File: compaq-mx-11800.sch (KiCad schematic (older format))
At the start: 246 parts, among them J1 Conn_01x16_Female, J2 Conn_01x16_Female, j1 MX-NoLED, k1 MX-NoLED, m1 MX-NoLED, p1 MX-NoLED, q1 MX-NoLED, t1 MX-NoLED, u1 MX-NoLED, x1 MX-NoLED, y1 MX-NoLED

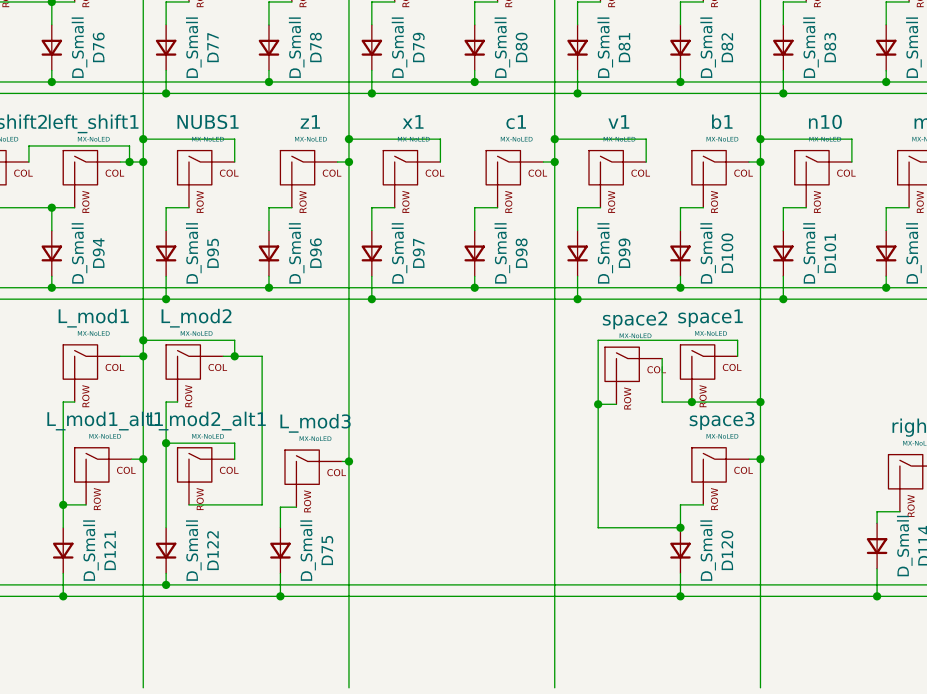
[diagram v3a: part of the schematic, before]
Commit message: revert to using MX_only
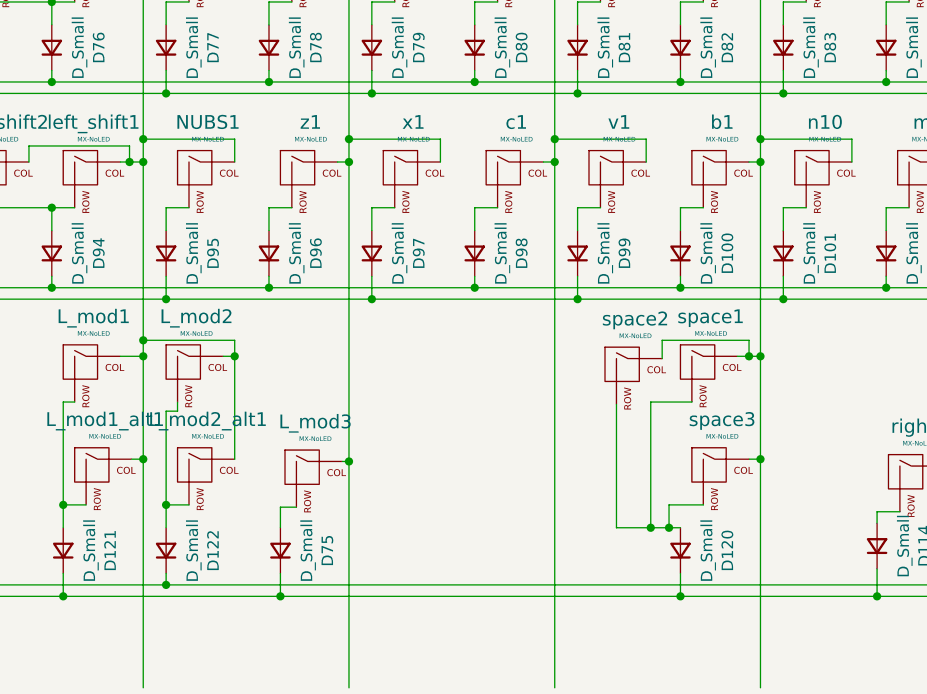
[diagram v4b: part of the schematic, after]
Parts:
- L_mod1, L_mod2, R_mod2, R_mod3: footprint MX_Alps_Hybrid:MX-1.5U-NoLED -> MX_Only:MXOnly-1.5U-NoLED
- L_mod1_alt1, L_mod2_alt1, L_mod3, R_mod1, R_mod2_alt1, R_mod3_alt1: footprint MX_Alps_Hybrid:MX-1.25U-NoLED -> MX_Only:MXOnly-1.25U-NoLED
- space1: footprint MX_Alps_Hybrid:MX-7U-NoLED -> MX_Only:MXOnly-7U-NoLED
- space2, space3: footprint MX_Alps_Hybrid:MX-6.25U-NoLED -> MX_Only:MXOnly-6.25U-NoLED
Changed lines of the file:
@@
 F 0 "L_mod2" H 9483 13823 60  0000 C CNN
 F 1 "MX-NoLED" H 9483 13749 20  0000 C CNN
-F 2 "MX_Alps_Hybrid:MX-1.5U-NoLED" H 8825 13575 60  0001 C CNN
+F 2 "MX_Only:MXOnly-1.5U-NoLED" H 8825 13575 60  0001 C CNN
 F 3 "" H 8825 13575 60  0001 C CNN
 	1    9450 13600
@@
 F 0 "space1" H 11733 13823 60  0000 C CNN
 F 1 "MX-NoLED" H 11733 13749 20  0000 C CNN
-F 2 "MX_Alps_Hybrid:MX-7U-NoLED" H 11075 13575 60  0001 C CNN
+F 2 "MX_Only:MXOnly-7U-NoLED" H 11075 13575 60  0001 C CNN
 F 3 "" H 11075 13575 60  0001 C CNN
 	1    11700 13600
@@
 F 0 "space3" H 11783 14273 60  0000 C CNN
 F 1 "MX-NoLED" H 11783 14199 20  0000 C CNN
-F 2 "MX_Alps_Hybrid:MX-6.25U-NoLED" H 11125 14025 60  0001 C CNN
+F 2 "MX_Only:MXOnly-6.25U-NoLED" H 11125 14025 60  0001 C CNN
 F 3 "" H 11125 14025 60  0001 C CNN
 	1    11750 14050
@@
 F 0 "R_mod1" H 13583 14223 60  0000 C CNN
 F 1 "MX-NoLED" H 13583 14149 20  0000 C CNN
-F 2 "MX_Alps_Hybrid:MX-1.25U-NoLED" H 12925 13975 60  0001 C CNN
+F 2 "MX_Only:MXOnly-1.25U-NoLED" H 12925 13975 60  0001 C CNN
 F 3 "" H 12925 13975 60  0001 C CNN
 	1    13550 14000
@@
 F 0 "R_mod2_alt1" H 14033 14223 60  0000 C CNN
 F 1 "MX-NoLED" H 14033 14149 20  0000 C CNN
-F 2 "MX_Alps_Hybrid:MX-1.25U-NoLED" H 13375 13975 60  0001 C CNN
+F 2 "MX_Only:MXOnly-1.25U-NoLED" H 13375 13975 60  0001 C CNN
 F 3 "" H 13375 13975 60  0001 C CNN
 	1    14000 14000
@@
 	14350 10350 14250 10350
 Wire Wire Line
-	9400 13750 9350 13750
-Wire Wire Line
 	13750 12700 13750 13430
 Wire Wire Line
@@
 F 0 "R_mod3_alt1" H 14943 14373 60  0000 C CNN
 F 1 "MX-NoLED" H 14943 14299 20  0000 C CNN
-F 2 "MX_Alps_Hybrid:MX-1.25U-NoLED" H 14285 14125 60  0001 C CNN
+F 2 "MX_Only:MXOnly-1.25U-NoLED" H 14285 14125 60  0001 C CNN
 F 3 "" H 14285 14125 60  0001 C CNN
 	1    14910 14150
@@
 F 0 "R_mod2" H 14013 13823 60  0000 C CNN
 F 1 "MX-NoLED" H 14013 13749 20  0000 C CNN
-F 2 "MX_Alps_Hybrid:MX-1.5U-NoLED" H 13355 13575 60  0001 C CNN
+F 2 "MX_Only:MXOnly-1.5U-NoLED" H 13355 13575 60  0001 C CNN
 F 3 "" H 13355 13575 60  0001 C CNN
 	1    13980 13600
@@
 F 0 "R_mod3" H 14933 13973 60  0000 C CNN
 F 1 "MX-NoLED" H 14933 13899 20  0000 C CNN
-F 2 "MX_Alps_Hybrid:MX-1.5U-NoLED" H 14275 13725 60  0001 C CNN
+F 2 "MX_Only:MXOnly-1.5U-NoLED" H 14275 13725 60  0001 C CNN
 F 3 "" H 14275 13725 60  0001 C CNN
 	1    14900 13750
@@
 F 0 "L_mod1" H 9033 13823 60  0000 C CNN
 F 1 "MX-NoLED" H 9033 13749 20  0000 C CNN
-F 2 "MX_Alps_Hybrid:MX-1.5U-NoLED" H 8375 13575 60  0001 C CNN
+F 2 "MX_Only:MXOnly-1.5U-NoLED" H 8375 13575 60  0001 C CNN
 F 3 "" H 8375 13575 60  0001 C CNN
 	1    9000 13600
@@
 F 0 "L_mod1_alt1" H 9083 14273 60  0000 C CNN
 F 1 "MX-NoLED" H 9083 14199 20  0000 C CNN
-F 2 "MX_Alps_Hybrid:MX-1.25U-NoLED" H 8425 14025 60  0001 C CNN
+F 2 "MX_Only:MXOnly-1.25U-NoLED" H 8425 14025 60  0001 C CNN
 F 3 "" H 8425 14025 60  0001 C CNN
 	1    9050 14050
@@
 F 0 "L_mod2_alt1" H 9533 14273 60  0000 C CNN
 F 1 "MX-NoLED" H 9533 14199 20  0000 C CNN
-F 2 "MX_Alps_Hybrid:MX-1.25U-NoLED" H 8875 14025 60  0001 C CNN
+F 2 "MX_Only:MXOnly-1.25U-NoLED" H 8875 14025 60  0001 C CNN
 F 3 "" H 8875 14025 60  0001 C CNN
 	1    9500 14050
@@
 Wire Wire Line
 	9250 13480 9250 13550
-Wire Wire Line
-	9350 13750 9350 13930
-Wire Wire Line
-	9450 14200 9770 14200
-Wire Wire Line
-	9770 14200 9770 13550
-Wire Wire Line
-	9770 13550 9650 13550
-Connection ~ 9650 13550
-Wire Wire Line
-	9650 14000 9650 13930
-Wire Wire Line
-	9650 13930 9350 13930
-Connection ~ 9350 13930
-Wire Wire Line
-	9350 13930 9350 14300
 $Comp
 L Device:D_Small D75
@@
 F 0 "L_mod3" H 10003 14283 60  0000 C CNN
 F 1 "MX-NoLED" H 10003 14209 20  0000 C CNN
-F 2 "MX_Alps_Hybrid:MX-1.25U-NoLED" H 9345 14035 60  0001 C CNN
+F 2 "MX_Only:MXOnly-1.25U-NoLED" H 9345 14035 60  0001 C CNN
 F 3 "" H 9345 14035 60  0001 C CNN
 	1    9970 14060
@@
 F 0 "space2" H 11403 13833 60  0000 C CNN
 F 1 "MX-NoLED" H 11403 13759 20  0000 C CNN
-F 2 "MX_Alps_Hybrid:MX-6.25U-NoLED" H 10745 13585 60  0001 C CNN
+F 2 "MX_Only:MXOnly-6.25U-NoLED" H 10745 13585 60  0001 C CNN
 F 3 "" H 10745 13585 60  0001 C CNN
 	1    11370 13610
 	1    0    0    -1
 $EndComp
-Connection ~ 11950 13750
-Wire Wire Line
-	11950 13750 11950 14000
-Wire Wire Line
-	11520 13560 11520 13750
-Wire Wire Line
-	11520 13750 11650 13750
-Connection ~ 11650 13750
-Wire Wire Line
-	11650 13750 11950 13750
 Wire Wire Line
 	11900 14000 11950 14000
@@
 	11950 14000 11950 15000
 Wire Wire Line
-	11600 14300 11240 14300
-Wire Wire Line
-	11240 14300 11240 13760
-Wire Wire Line
-	11240 13480 11850 13480
-Wire Wire Line
-	11850 13550 11850 13480
-Wire Wire Line
-	11320 13760 11240 13760
-Connection ~ 11240 13760
-Wire Wire Line
-	11240 13760 11240 13480
-Wire Wire Line
-	11700 14200 11600 14200
-Wire Wire Line
-	11600 14200 11600 14300
-Connection ~ 11600 14300
+	11600 14300 11550 14300
 Wire Wire Line
-	11950 12700 11950 13750
+	11950 12700 11950 13550
 Wire Wire Line
 	8200 14550 9350 14550
@@
 Wire Wire Line
 	8900 8650 10250 8650
+Wire Wire Line
+	9400 13750 9400 13790
+Wire Wire Line
+	9400 13790 9350 13790
+Wire Wire Line
+	9450 14200 9350 14200
+Wire Wire Line
+	9350 13790 9350 14200
+Connection ~ 9350 14200
+Wire Wire Line
+	9350 14200 9350 14300
+Wire Wire Line
+	9650 14000 9650 13550
+Connection ~ 9650 13550
+Wire Wire Line
+	11850 13550 11900 13550
+Connection ~ 11950 13550
+Wire Wire Line
+	11950 13550 11950 14000
+Wire Wire Line
+	11520 13560 11520 13480
+Wire Wire Line
+	11320 13760 11320 14300
+Wire Wire Line
+	11650 13750 11470 13750
+Wire Wire Line
+	11470 13750 11470 14300
+Connection ~ 11470 14300
+Wire Wire Line
+	11470 14300 11320 14300
+Wire Wire Line
+	11700 14200 11550 14200
+Wire Wire Line
+	11550 14200 11550 14300
+Connection ~ 11550 14300
+Wire Wire Line
+	11550 14300 11470 14300
+Wire Wire Line
+	11900 13480 11900 13550
+Wire Wire Line
+	11520 13480 11900 13480
+Connection ~ 11900 13550
+Wire Wire Line
+	11900 13550 11950 13550
 $EndSCHEMATC

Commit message: update diode footprint
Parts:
- D10, D100, D101, D102, D103, D104, D105, D107, D108, D11, D114, D115, D116, D117, D118, D12, D120, D121, D122, D124, D13, D14, D15, D16, D18, D19, D2, D20, D21, D22, D23, D24, D25, D26, D27, D28, D29, D3, D30, D31, D32, D33, D34, D35, D36, D37, D38, D39, D4, D40, D41, D42, D43, D44, D45, D46, D47, D48, D49, D5, D51, D53, D54, D55, D56, D57, D58, D59, D6, D60, D61, D62, D63, D64, D65, D66, D67, D68, D69, D7, D70, D71, D72, D73, D74, D75, D76, D77, D78, D79, D8, D80, D81, D82, D83, D84, D85, D86, D87, D88, D9, D91, D92, D94, D95, D96, D97, D98, D99: footprint Keebio-Parts:Diode-dual -> vuckale:Diode

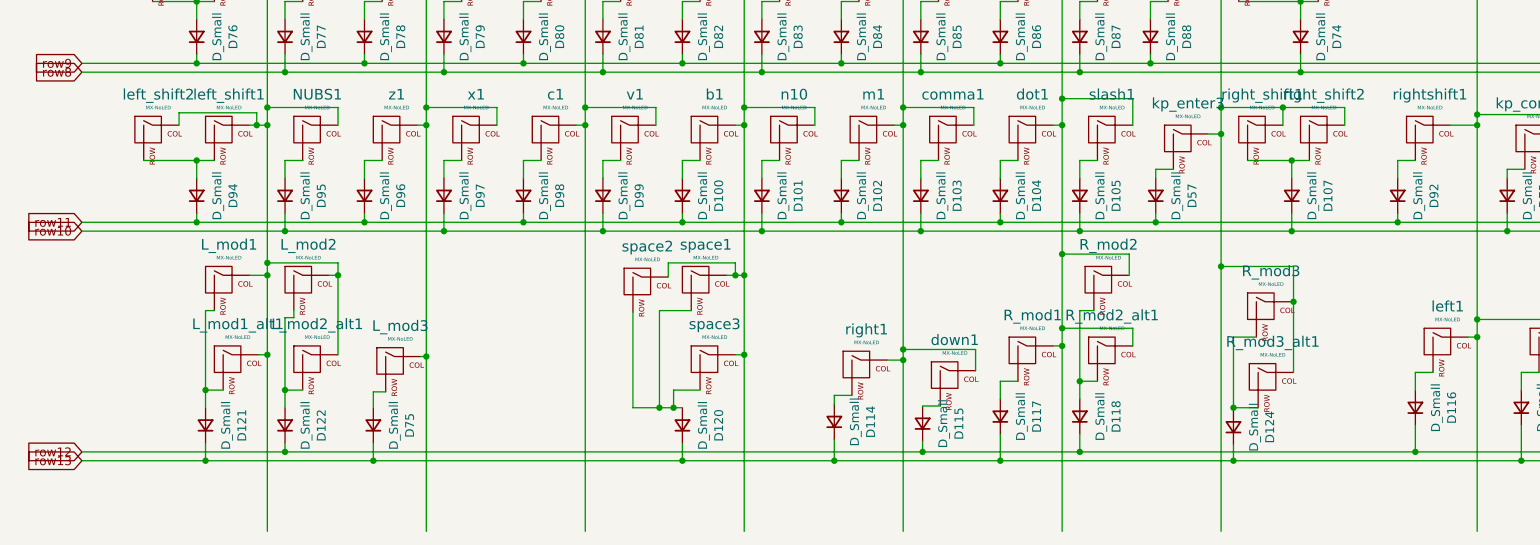
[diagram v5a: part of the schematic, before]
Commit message: add 1u-1u-1u-7u-1u-1u-1u support for bottom row
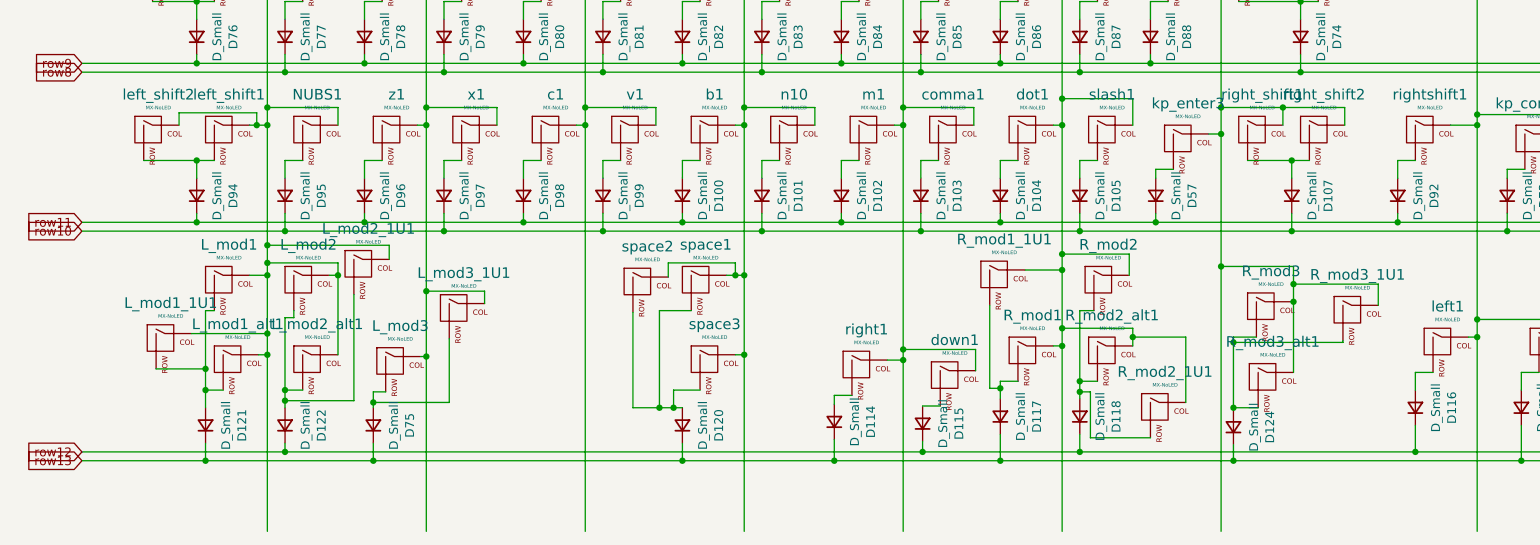
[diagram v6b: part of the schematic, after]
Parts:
- added L_mod1_1U1, L_mod2_1U1, L_mod3_1U1, R_mod1_1U1, R_mod2_1U1, R_mod3_1U1: MX-NoLED, MX_Only:MXOnly-1U-NoLED, symbol MX_Alps_Hybrid:MX-NoLED
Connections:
- wire segments 797 -> 831
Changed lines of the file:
@@
 $EndComp
 Wire Wire Line
-	13850 14150 13850 14250
+	13850 14150 13850 14210
 Wire Wire Line
 	13950 14150 13850 14150
@@
 Connection ~ 8850 12000
 Wire Wire Line
-	13400 14150 13400 14250
+	13400 14150 13400 14190
 Wire Wire Line
 	8550 12900 8850 12900
@@
 Connection ~ 13750 12700
 Wire Wire Line
-	14150 13950 14150 13850
+	14150 13950 14150 13900
 Wire Wire Line
 	14150 12700 14150 12550
@@
 	13400 9050 13400 9100
 Wire Wire Line
-	10150 12700 10150 14010
-Wire Wire Line
 	16270 13000 16270 12950
 Wire Wire Line
@@
 Connection ~ 13750 13430
 Wire Wire Line
-	13750 13430 13750 13850
+	13750 13430 13750 13520
 Wire Wire Line
 	13930 13750 13850 13750
@@
 Wire Wire Line
 	14850 13900 14720 13900
-Wire Wire Line
-	14720 13900 14720 14300
 Connection ~ 14720 14300
 Wire Wire Line
@@
 	15060 14100 15060 13700
 Wire Wire Line
-	15060 13700 15060 13500
-Wire Wire Line
 	14650 13500 15060 13500
 Connection ~ 15060 13700
@@
 $EndComp
 Wire Wire Line
-	9250 12700 9250 13480
+	9250 12700 9250 13380
 Wire Wire Line
 	9200 14000 9250 14000
@@
 Connection ~ 9250 13550
 Wire Wire Line
-	9250 13550 9250 14000
-Wire Wire Line
 	8950 13750 8900 13750
 Wire Wire Line
-	8900 13750 8900 14200
-Wire Wire Line
 	9000 14200 8900 14200
 Connection ~ 8900 14200
@@
 	9920 14210 9850 14210
 Wire Wire Line
-	9850 14210 9850 14300
+	9850 14210 9850 14270
 Wire Wire Line
 	10120 14010 10150 14010
@@
 	13400 14600 14720 14600
 Wire Wire Line
-	13850 14450 13850 14550
-Wire Wire Line
 	12960 14550 13850 14550
 Connection ~ 13850 14550
@@
 Connection ~ 9350 14200
 Wire Wire Line
-	9350 14200 9350 14300
-Wire Wire Line
-	9650 14000 9650 13550
+	9350 14200 9350 14260
 Connection ~ 9650 13550
 Wire Wire Line
@@
 Wire Wire Line
 	11900 13550 11950 13550
+$Comp
+L MX_Alps_Hybrid:MX-NoLED L_mod1_1U1
+U 1 1 6207D6A4
+P 8670 13930
+F 0 "L_mod1_1U1" H 8703 14153 60  0000 C CNN
+F 1 "MX-NoLED" H 8703 14079 20  0000 C CNN
+F 2 "MX_Only:MXOnly-1U-NoLED" H 8045 13905 60  0001 C CNN
+F 3 "" H 8045 13905 60  0001 C CNN
+	1    8670 13930
+	1    0    0    -1
+$EndComp
+Wire Wire Line
+	9250 13550 9250 13880
+Wire Wire Line
+	8820 13880 9250 13880
+Connection ~ 9250 13880
+Wire Wire Line
+	9250 13880 9250 14000
+Wire Wire Line
+	8620 14080 8900 14080
+Wire Wire Line
+	8900 13750 8900 14080
+Connection ~ 8900 14080
+Wire Wire Line
+	8900 14080 8900 14200
+$Comp
+L MX_Alps_Hybrid:MX-NoLED L_mod2_1U1
+U 1 1 6232C08A
+P 9790 13510
+F 0 "L_mod2_1U1" H 9823 13733 60  0000 C CNN
+F 1 "MX-NoLED" H 9823 13659 20  0000 C CNN
+F 2 "MX_Only:MXOnly-1U-NoLED" H 9165 13485 60  0001 C CNN
+F 3 "" H 9165 13485 60  0001 C CNN
+	1    9790 13510
+	1    0    0    -1
+$EndComp
+Wire Wire Line
+	9940 13460 9940 13380
+Wire Wire Line
+	9940 13380 9250 13380
+Connection ~ 9250 13380
+Wire Wire Line
+	9250 13380 9250 13480
+$Comp
+L MX_Alps_Hybrid:MX-NoLED L_mod3_1U1
+U 1 1 62527DE9
+P 10330 13760
+F 0 "L_mod3_1U1" H 10363 13983 60  0000 C CNN
+F 1 "MX-NoLED" H 10363 13909 20  0000 C CNN
+F 2 "MX_Only:MXOnly-1U-NoLED" H 9705 13735 60  0001 C CNN
+F 3 "" H 9705 13735 60  0001 C CNN
+	1    10330 13760
+	1    0    0    -1
+$EndComp
+Wire Wire Line
+	10150 12700 10150 13640
+Wire Wire Line
+	10480 13710 10480 13640
+Wire Wire Line
+	10480 13640 10150 13640
+Connection ~ 10150 13640
+Wire Wire Line
+	9650 13550 9650 14000
+Wire Wire Line
+	9740 13660 9740 14260
+Wire Wire Line
+	9740 14260 9350 14260
+Connection ~ 9350 14260
+Wire Wire Line
+	9350 14260 9350 14300
+Wire Wire Line
+	10150 13640 10150 14010
+Wire Wire Line
+	10280 13910 10280 14270
+Wire Wire Line
+	10280 14270 9850 14270
+Connection ~ 9850 14270
+Wire Wire Line
+	9850 14270 9850 14300
+$Comp
+L MX_Alps_Hybrid:MX-NoLED R_mod1_1U1
+U 1 1 628C2558
+P 13390 13570
+F 0 "R_mod1_1U1" H 13423 13793 60  0000 C CNN
+F 1 "MX-NoLED" H 13423 13719 20  0000 C CNN
+F 2 "MX_Only:MXOnly-1U-NoLED" H 12765 13545 60  0001 C CNN
+F 3 "" H 12765 13545 60  0001 C CNN
+	1    13390 13570
+	1    0    0    -1
+$EndComp
+Wire Wire Line
+	13540 13520 13750 13520
+Connection ~ 13750 13520
+Wire Wire Line
+	13750 13520 13750 13850
+Wire Wire Line
+	13340 13720 13340 14190
+Wire Wire Line
+	13340 14190 13400 14190
+Connection ~ 13400 14190
+Wire Wire Line
+	13400 14190 13400 14250
+$Comp
+L MX_Alps_Hybrid:MX-NoLED R_mod2_1U1
+U 1 1 62ADF745
+P 14300 14320
+F 0 "R_mod2_1U1" H 14333 14543 60  0000 C CNN
+F 1 "MX-NoLED" H 14333 14469 20  0000 C CNN
+F 2 "MX_Only:MXOnly-1U-NoLED" H 13675 14295 60  0001 C CNN
+F 3 "" H 13675 14295 60  0001 C CNN
+	1    14300 14320
+	1    0    0    -1
+$EndComp
+Wire Wire Line
+	14450 14270 14450 13900
+Wire Wire Line
+	14450 13900 14150 13900
+Connection ~ 14150 13900
+Wire Wire Line
+	14150 13900 14150 13850
+Wire Wire Line
+	13850 14450 13850 14550
+Wire Wire Line
+	14250 14470 13910 14470
+Wire Wire Line
+	13910 14470 13910 14210
+Wire Wire Line
+	13910 14210 13850 14210
+Connection ~ 13850 14210
+Wire Wire Line
+	13850 14210 13850 14250
+$Comp
+L MX_Alps_Hybrid:MX-NoLED R_mod3_1U1
+U 1 1 62DE4C5C
+P 15390 13770
+F 0 "R_mod3_1U1" H 15423 13993 60  0000 C CNN
+F 1 "MX-NoLED" H 15423 13919 20  0000 C CNN
+F 2 "MX_Only:MXOnly-1U-NoLED" H 14765 13745 60  0001 C CNN
+F 3 "" H 14765 13745 60  0001 C CNN
+	1    15390 13770
+	1    0    0    -1
+$EndComp
+Wire Wire Line
+	15340 13930 14720 13930
+Wire Wire Line
+	14720 13900 14720 13930
+Connection ~ 14720 13930
+Wire Wire Line
+	14720 13930 14720 14300
+Wire Wire Line
+	15060 13500 15060 13600
+Wire Wire Line
+	15540 13720 15540 13600
+Wire Wire Line
+	15540 13600 15060 13600
+Connection ~ 15060 13600
+Wire Wire Line
+	15060 13600 15060 13700
+Wire Wire Line
+	15340 13930 15340 13920
 $EndSCHEMATC

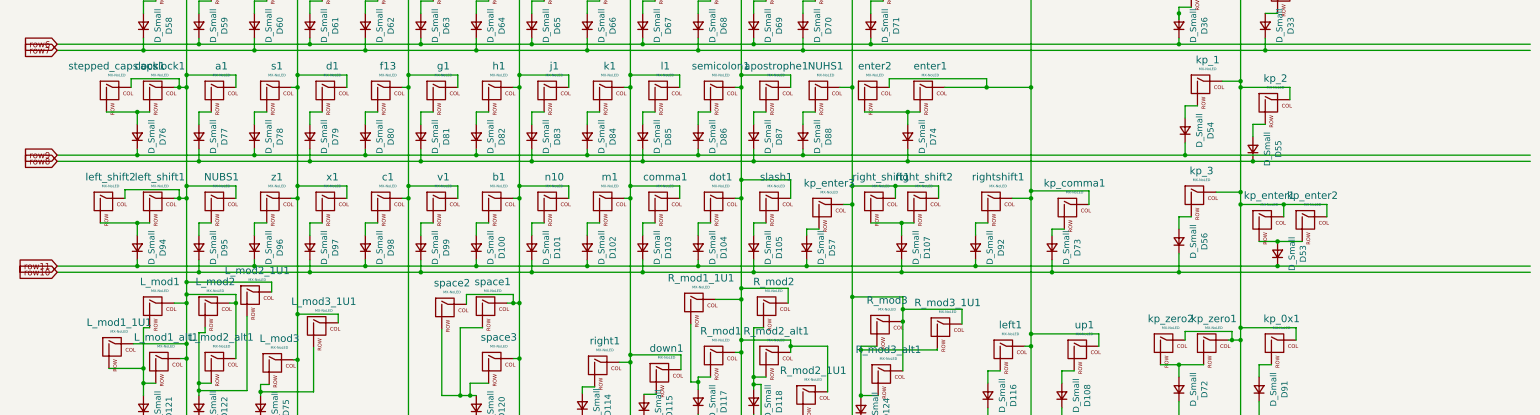
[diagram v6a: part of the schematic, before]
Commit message: fix scematic row col order
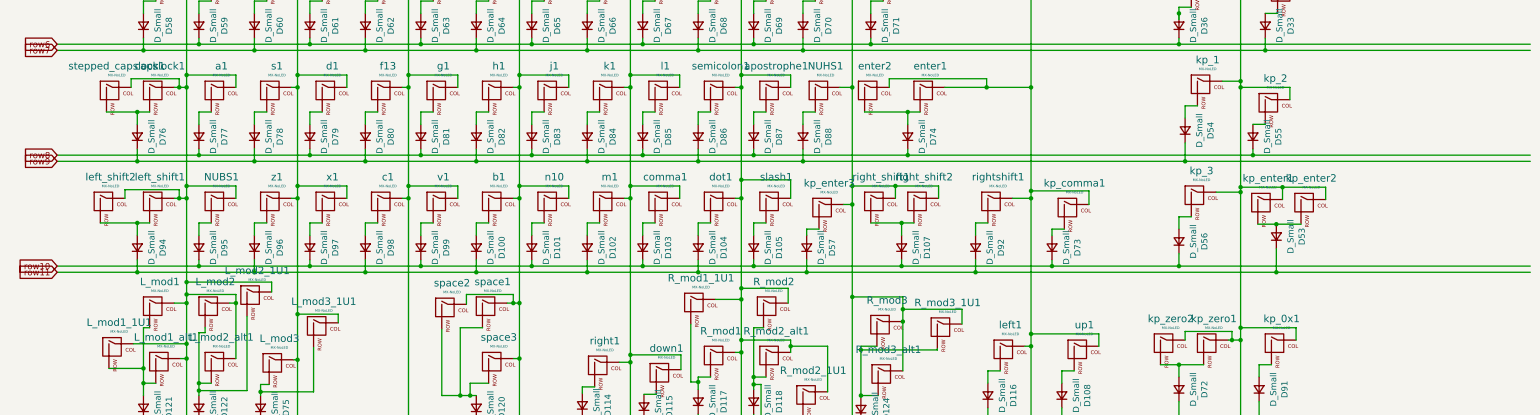
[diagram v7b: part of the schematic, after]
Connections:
- wire segments 831 -> 832
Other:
- moved on the sheet: D53, D55, kp_enter1, kp_enter2

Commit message: clean up schematics
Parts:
- renumbered L_mod1 to lm1, L_mod1_alt1 to lm1a, L_mod1_1U1 to lm1u, L_mod2 to lm2, L_mod2_1U1 to lm21u, L_mod2_alt1 to lm2a
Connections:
- wire segments 832 -> 823
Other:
- moved on the sheet: D118, D121, D122, D124, D75, L_mod3, L_mod3_1U1, R_mod1, R_mod1_1U1, R_mod2, R_mod2_1U1, R_mod2_alt1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
